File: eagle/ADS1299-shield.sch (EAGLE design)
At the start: 139 parts, among them IC1 ADS1299IPAG, IC2 TPS72325DBVT, IC3 TPS73225DBVT, IC5 24AA256UID, IC6 TPS60403DBVT, IC7 OPA376DBV, IC8 OPA376DBV, IC9 TXS0102DCUR, J16 EXTERNAL_SYNC, J8 Electrode Connector, U2 TXB0108PWR, U3 TXB0108PWR

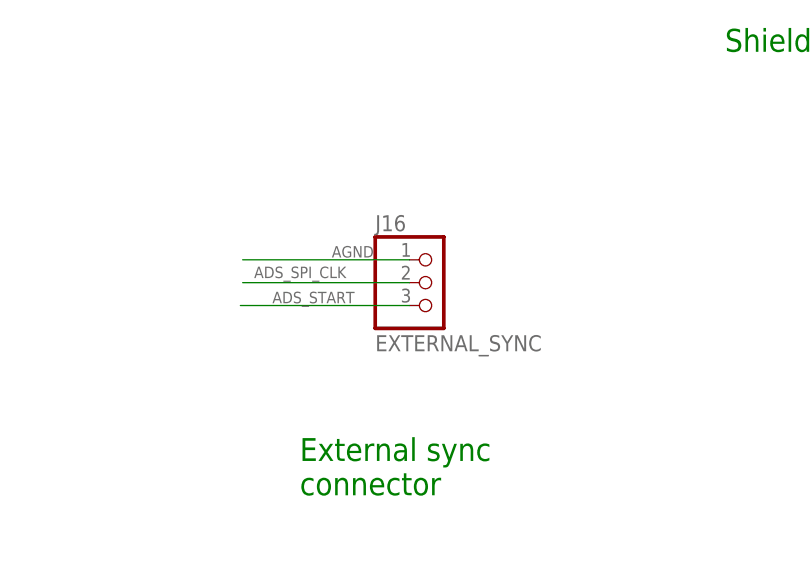
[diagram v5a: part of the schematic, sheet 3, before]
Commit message: made lable text bigger and repositioned; added Arduino pin labels; added 1uf cap to 2.5 power supple to match eval board; relabeled power and buffer 3-pin jumpers with numbers instead of letters, to match schematic; adjusted autoroute of XIO connector rotation change; adjusted trace widths various places
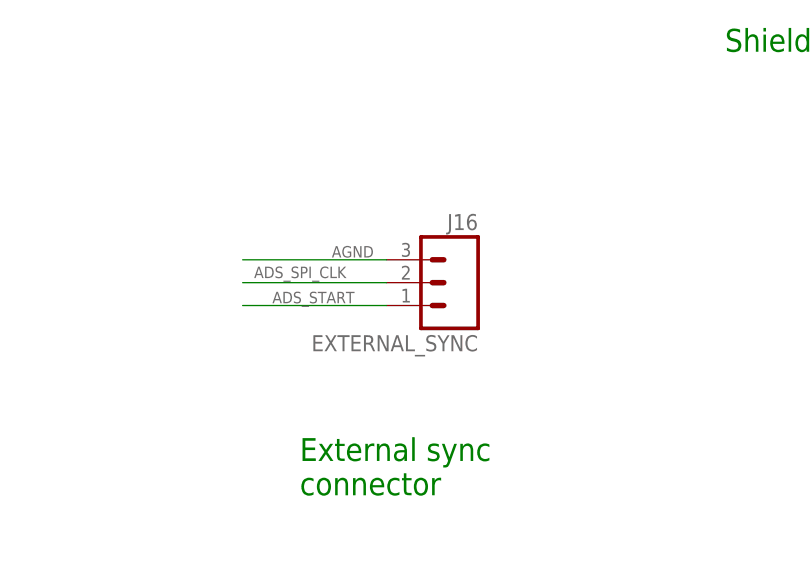
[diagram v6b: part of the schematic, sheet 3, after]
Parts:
- added C68: 1uF, SparkFun-Passives:CAP0603-CAP
- J16: device adafruit:JST_3PIN -> SparkFun-Connectors:M03JST-PTH
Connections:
- net AGND: now also C68.2
- net VCC_5V_FILTERED: now also C68.1
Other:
- moved on the sheet: J16
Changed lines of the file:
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@@
 <part name="R34" library="SparkFun-Passives" deviceset="RESISTOR" device="0603-RES" value="4.99k"/>
 <part name="SUPPLY51" library="supply2" deviceset="AGND" device=""/>
-<part name="J16" library="adafruit" deviceset="JST_3PIN" device="" value="EXTERNAL_SYNC"/>
+<part name="J16" library="SparkFun-Connectors" deviceset="M03" device="JST-PTH" value="EXTERNAL_SYNC"/>
 <part name="JP2" library="headers" deviceset="PINHD-2X10" device="" value="CONFIG0"/>
 <part name="R2" library="SparkFun-Passives" deviceset="RESISTOR" device="0603-RES" value="10k"/>
@@
 <part name="C66" library="SparkFun-Passives" deviceset="CAP" device="0603-CAP" value="0.01uF"/>
 <part name="R6" library="SparkFun-Passives" deviceset="RESISTOR" device="0603-RES" value="3.98K"/>
+<part name="SUPPLY16" library="supply2" deviceset="AGND" device=""/>
+<part name="C68" library="SparkFun-Passives" deviceset="CAP" device="0603-CAP" value="1uF"/>
 </parts>
 <sheets>
@@
 <attribute name="VALUE" x="287.274" y="119.888" size="1.778" layer="96" rot="R90"/>
 </instance>
+<instance part="SUPPLY16" gate="G$1" x="63.754" y="73.406"/>
+<instance part="C68" gate="G$1" x="63.754" y="80.772"/>
 </instances>
 <busses>
@@
 <wire x1="81.788" y1="124.206" x2="76.962" y2="124.206" width="0.1524" layer="91"/>
 <junction x="76.962" y="124.206"/>
+</segment>
+<segment>
+<pinref part="C68" gate="G$1" pin="2"/>
+<pinref part="SUPPLY16" gate="G$1" pin="AGND"/>
+<wire x1="63.754" y1="75.946" x2="63.754" y2="78.232" width="0.1524" layer="91"/>
 </segment>
 </net>
@@
 <pinref part="IC3" gate="G$1" pin="IN"/>
 <wire x1="79.756" y1="90.424" x2="72.898" y2="90.424" width="0.1524" layer="91"/>
-<label x="48.006" y="87.63" size="1.778" layer="95"/>
+<label x="66.04" y="106.934" size="1.778" layer="95"/>
 <wire x1="72.898" y1="90.424" x2="63.754" y2="90.424" width="0.1524" layer="91"/>
 <wire x1="72.898" y1="90.424" x2="72.898" y2="85.344" width="0.1524" layer="91"/>
@@
 <junction x="81.788" y="141.986"/>
 <pinref part="C65" gate="G$1" pin="1"/>
+<pinref part="C68" gate="G$1" pin="1"/>
+<wire x1="63.754" y1="90.424" x2="63.754" y2="85.852" width="0.1524" layer="91"/>
+<junction x="63.754" y="90.424"/>
 </segment>
 </net>
@@
 <attribute name="VALUE" x="16.383" y="180.721" size="1.778" layer="96" rot="R180"/>
 </instance>
-<instance part="J16" gate="G$1" x="282.956" y="58.928"/>
+<instance part="J16" gate="G$1" x="285.496" y="58.928" rot="MR0"/>
 <instance part="JP2" gate="A" x="121.92" y="45.974"/>
 <instance part="R2" gate="G$1" x="25.908" y="226.822" smashed="yes">
@@
 </segment>
 <segment>
-<wire x1="280.416" y1="61.468" x2="261.874" y2="61.468" width="0.1524" layer="91"/>
+<wire x1="277.876" y1="56.388" x2="261.874" y2="56.388" width="0.1524" layer="91"/>
 <label x="271.78" y="61.722" size="1.27" layer="95"/>
 <pinref part="J16" gate="G$1" pin="1"/>
@@
 </segment>
 <segment>
-<wire x1="280.416" y1="58.928" x2="261.874" y2="58.928" width="0.1524" layer="91"/>
+<wire x1="277.876" y1="58.928" x2="261.874" y2="58.928" width="0.1524" layer="91"/>
 <label x="263.144" y="59.436" size="1.27" layer="95"/>
 <pinref part="J16" gate="G$1" pin="2"/>
@@
 <segment>
 <pinref part="J16" gate="G$1" pin="3"/>
-<wire x1="280.416" y1="56.388" x2="261.62" y2="56.388" width="0.1524" layer="91"/>
+<wire x1="277.876" y1="61.468" x2="261.874" y2="61.468" width="0.1524" layer="91"/>
 <label x="265.176" y="56.642" size="1.27" layer="95"/>
 </segment>

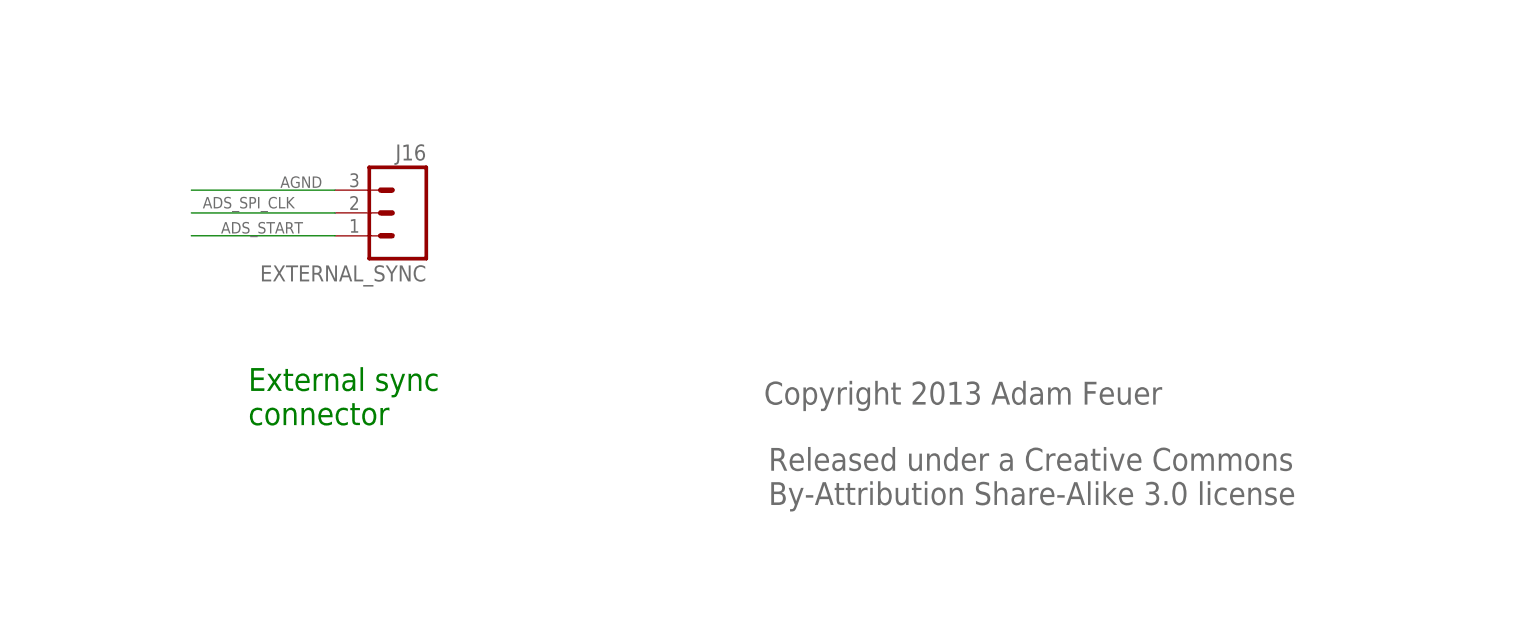
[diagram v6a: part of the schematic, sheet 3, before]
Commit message: minor updates to trace clearances; moved logos on bottom of board so the don't cover the copyright
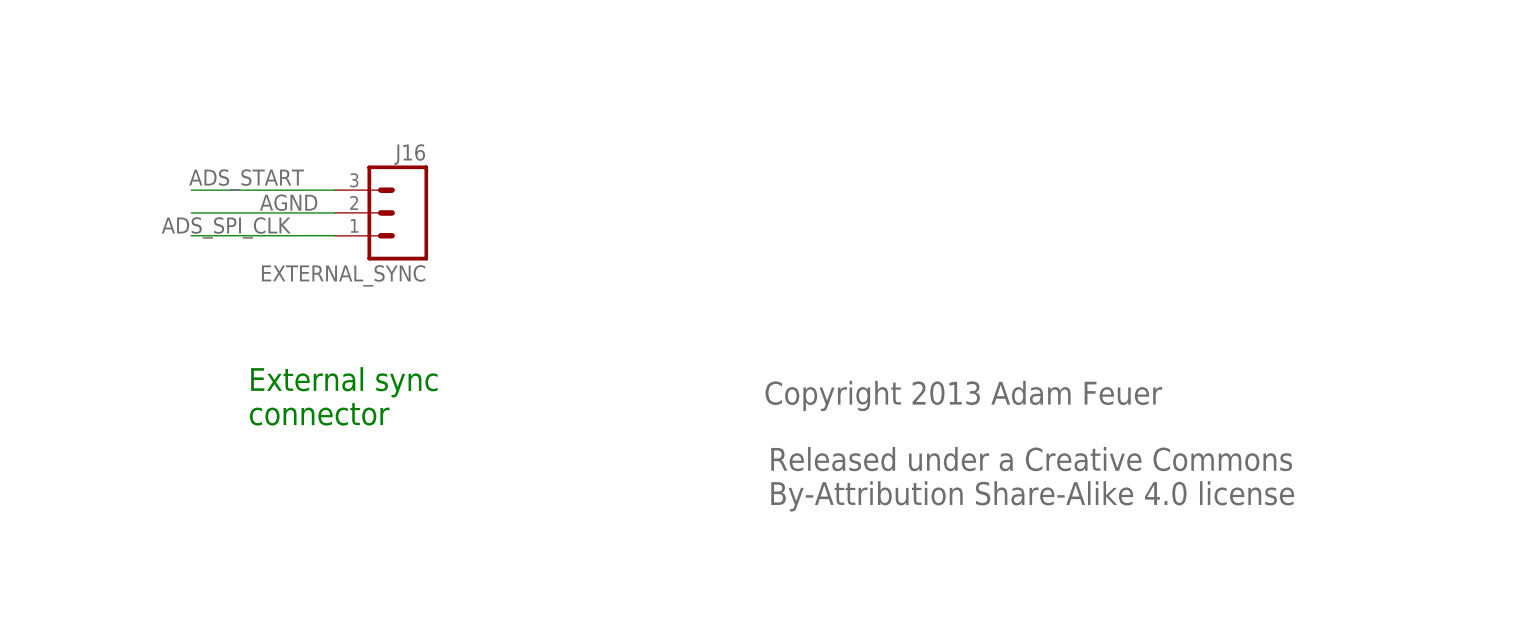
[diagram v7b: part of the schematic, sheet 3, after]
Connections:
- net ADS_SPI_CLK: now also J16.1; no longer J16.2
- net AGND: now also J16.2; no longer J16.1
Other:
- note added: "Released under a Creative Commons By-Attribution Share-Alike 4.0 license"
- note removed: "Released under a Creative Commons By-Attribution Share-Alike 3.0 license"
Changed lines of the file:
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@@
 <text x="246.634" y="215.392" size="1.778" layer="91">NC</text>
 <text x="329.184" y="26.416" size="2.54" layer="95">Released under a Creative Commons
-By-Attribution Share-Alike 3.0 license</text>
+By-Attribution Share-Alike 4.0 license</text>
 <text x="328.676" y="37.592" size="2.54" layer="95">Copyright 2013 Adam Feuer</text>
 <text x="416.306" y="7.112" size="2.1844" layer="95">v1.0</text>
@@
 <text x="293.116" y="179.324" size="2.54" layer="91">Bias</text>
 <text x="320.802" y="26.416" size="2.54" layer="95">Released under a Creative Commons
-By-Attribution Share-Alike 3.0 license</text>
+By-Attribution Share-Alike 4.0 license</text>
 <text x="320.294" y="37.592" size="2.54" layer="95">Copyright 2013 Adam Feuer</text>
 </plain>
@@
 jumper storage)</text>
 <text x="326.136" y="26.416" size="2.54" layer="95">Released under a Creative Commons
-By-Attribution Share-Alike 3.0 license</text>
+By-Attribution Share-Alike 4.0 license</text>
 <text x="325.628" y="37.592" size="2.54" layer="95">Copyright 2013 Adam Feuer</text>
 <text x="315.468" y="84.582" size="2.54" layer="91">Shield Connectors</text>
@@
 </segment>
 <segment>
-<wire x1="277.876" y1="56.388" x2="261.874" y2="56.388" width="0.1524" layer="91"/>
-<label x="271.78" y="61.722" size="1.27" layer="95"/>
-<pinref part="J16" gate="G$1" pin="1"/>
+<wire x1="277.876" y1="58.928" x2="261.874" y2="58.928" width="0.1524" layer="91"/>
+<pinref part="J16" gate="G$1" pin="2"/>
+<label x="269.494" y="59.182" size="1.778" layer="95"/>
 </segment>
 </net>
@@
 </segment>
 <segment>
-<wire x1="277.876" y1="58.928" x2="261.874" y2="58.928" width="0.1524" layer="91"/>
-<label x="263.144" y="59.436" size="1.27" layer="95"/>
-<pinref part="J16" gate="G$1" pin="2"/>
-</segment>
-<segment>
 <pinref part="U2" gate="G$1" pin="B4"/>
 <wire x1="64.77" y1="211.582" x2="78.486" y2="211.582" width="0.1524" layer="91"/>
 <label x="67.564" y="211.836" size="1.778" layer="95"/>
+</segment>
+<segment>
+<wire x1="277.876" y1="56.388" x2="261.874" y2="56.388" width="0.1524" layer="91"/>
+<pinref part="J16" gate="G$1" pin="1"/>
+<label x="258.572" y="56.642" size="1.778" layer="95"/>
 </segment>
 </net>
@@
 <pinref part="J16" gate="G$1" pin="3"/>
 <wire x1="277.876" y1="61.468" x2="261.874" y2="61.468" width="0.1524" layer="91"/>
-<label x="265.176" y="56.642" size="1.27" layer="95"/>
-</segment>
-</net>
+<label x="261.62" y="61.976" size="1.778" layer="95"/>
+</segment>
+</net>

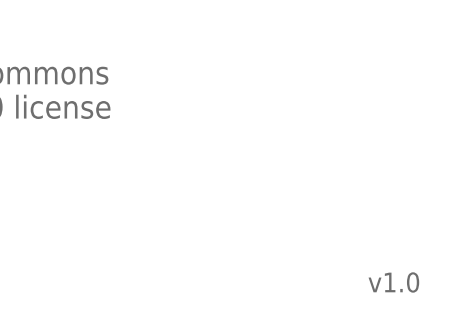
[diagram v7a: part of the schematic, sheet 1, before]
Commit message: minor updates to component labels
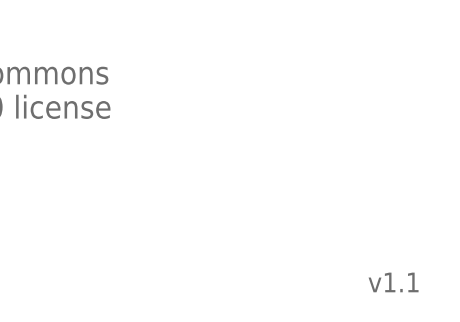
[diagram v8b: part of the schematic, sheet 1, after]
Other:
- note added: "v1.1"
- note removed: "v1.0"
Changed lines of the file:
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@@
 By-Attribution Share-Alike 4.0 license</text>
 <text x="328.676" y="37.592" size="2.54" layer="95">Copyright 2013 Adam Feuer</text>
-<text x="416.306" y="7.112" size="2.1844" layer="95">v1.0</text>
+<text x="416.306" y="7.112" size="2.1844" layer="95">v1.1</text>
 <text x="246.634" y="212.344" size="1.778" layer="91">NC</text>
 <text x="327.406" y="161.798" size="1.27" layer="91">NC</text>
